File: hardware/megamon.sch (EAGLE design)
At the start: 76 parts

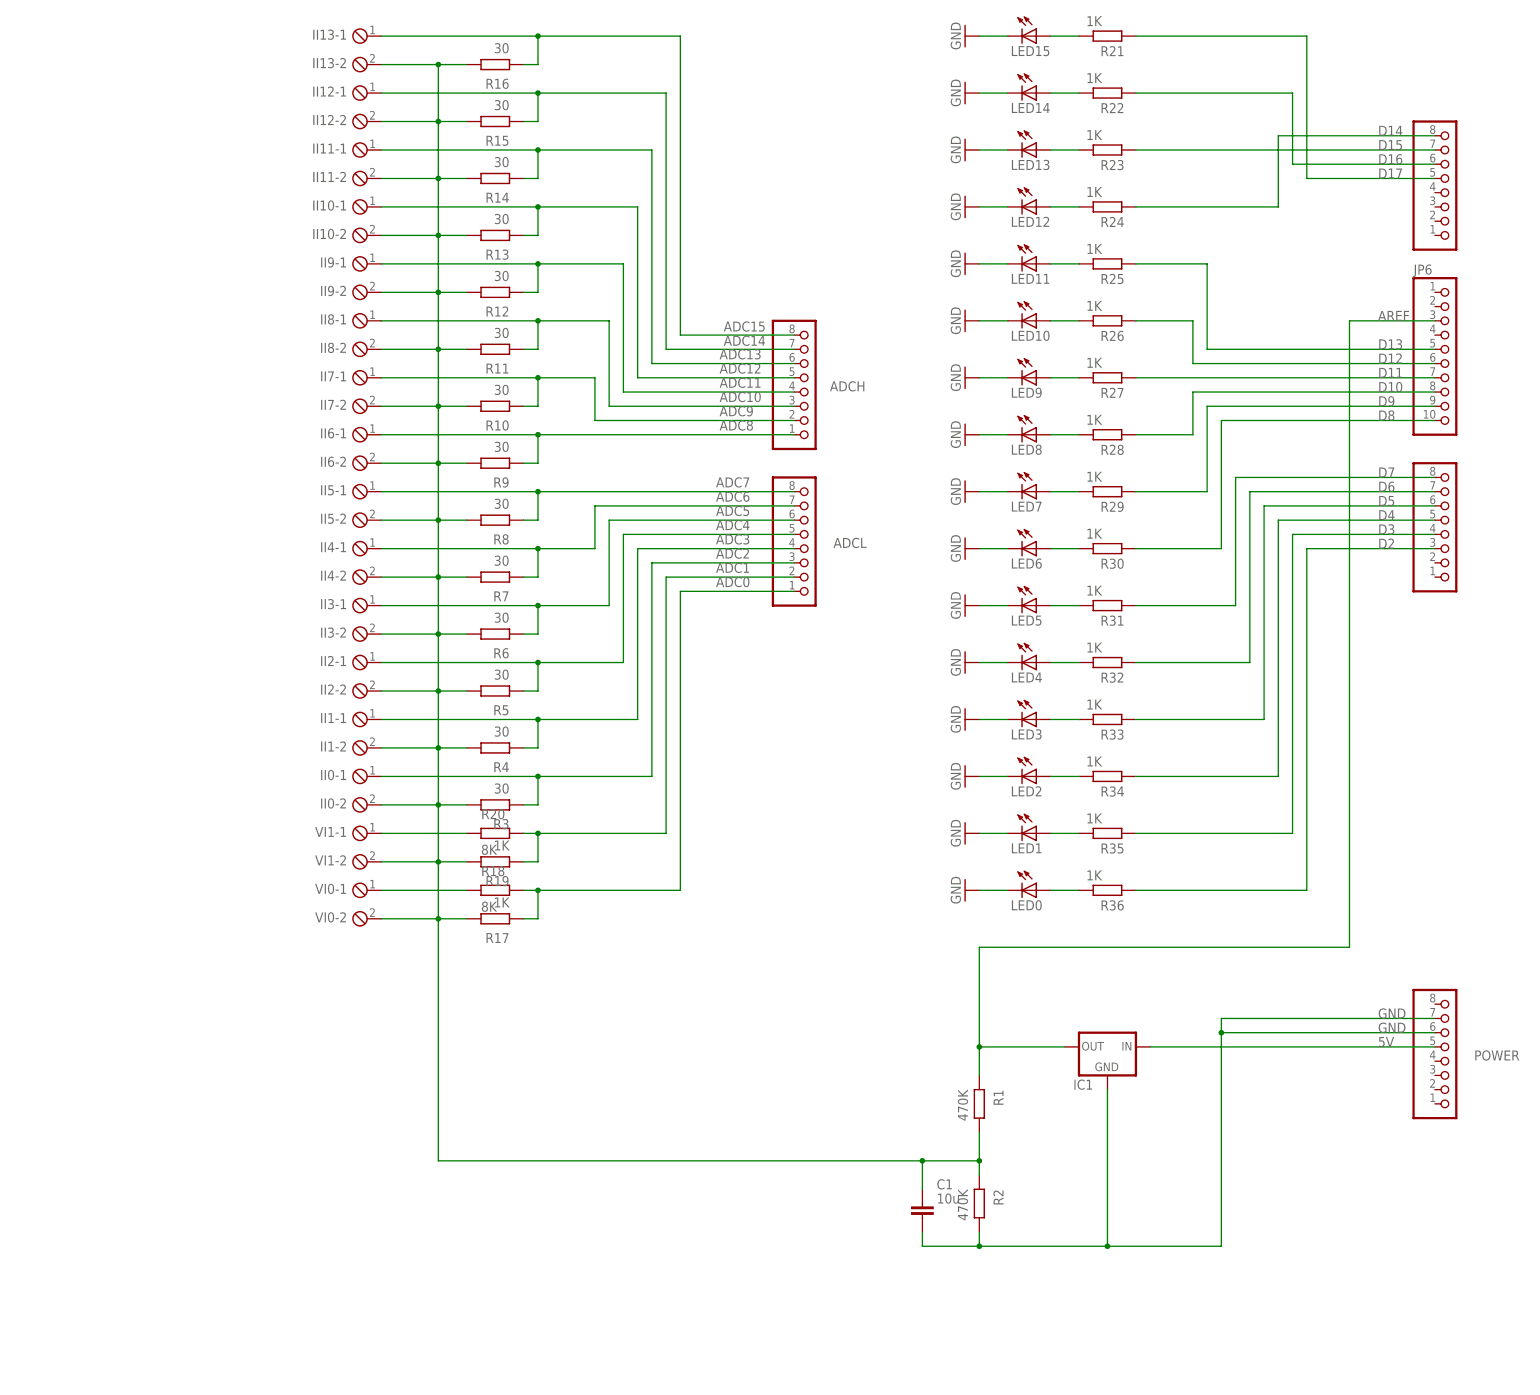
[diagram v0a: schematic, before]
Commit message: replace ngspice components with real ones
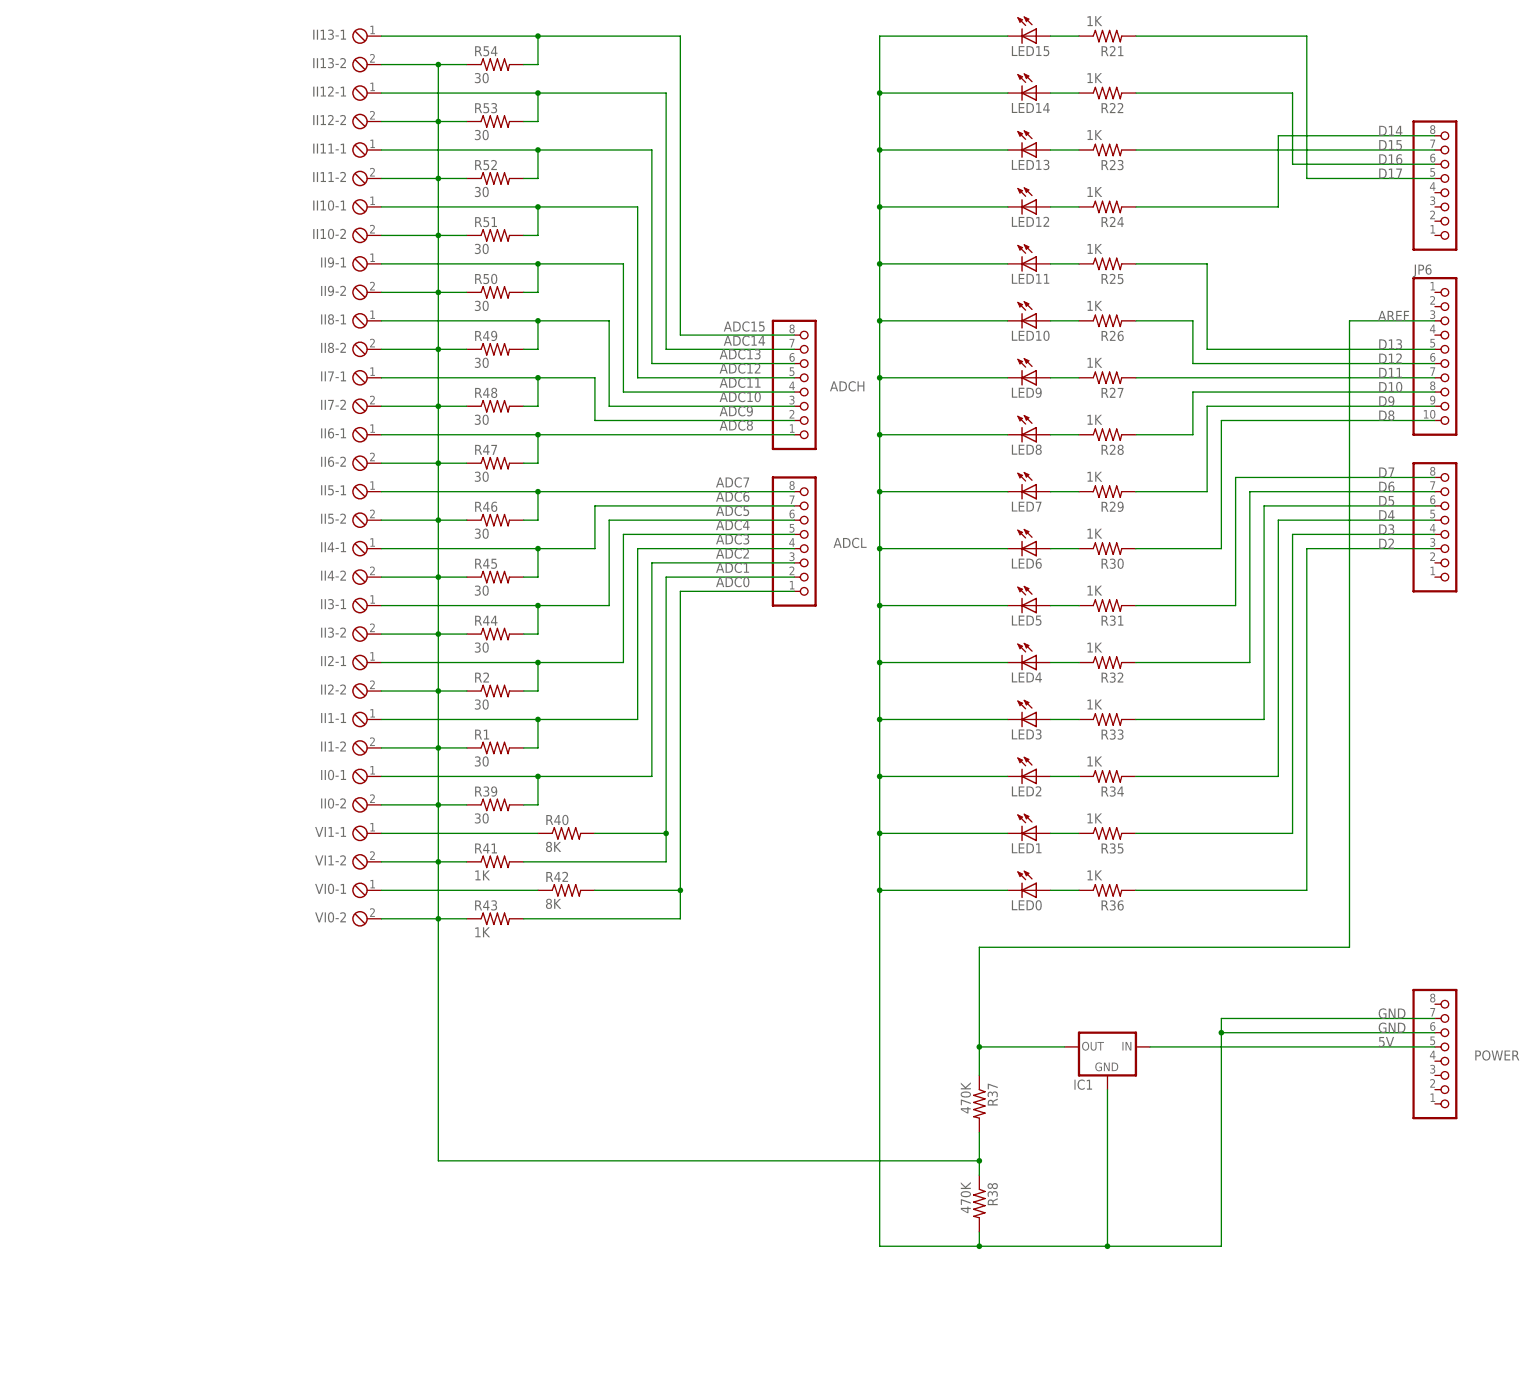
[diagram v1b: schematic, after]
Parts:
- removed C1: 10u, ngspice-simulation:C
- removed R10, R11, R12, R13, R14, R15, R16, R3, R4, R5, R6, R7, R8, R9: 30, ngspice-simulation:R
- removed R17, R19: 1K, ngspice-simulation:R
- removed R18, R20: 8K, ngspice-simulation:R
- added R37, R38: 470K, rcl:R-US_0204/7
- added R39, R44, R45, R46, R47, R48, R49, R50, R51, R52, R53, R54: 30, rcl:R-US_0204/7
- added R40, R42: 8K, rcl:R-US_0204/7
- added R41, R43: 1K, rcl:R-US_0204/7
- LED0, LED1, LED10, LED11, LED12, LED13, LED14, LED15, LED2, LED3, LED4, LED5, LED6, LED7, LED8, LED9: device led:LEDCHIPLED_0805 -> adafruit:LED3MM
- R1, R2: value 470K -> 30; device ngspice-simulation:R -> rcl:R-US_0204/7
- R21, R22, R23, R24, R25, R26, R27, R28, R29, R30, R31, R32, R33, R34, R35, R36: device rcl:R-EU_R0603 -> rcl:R-US_0204/7
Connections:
- net ADC0: now also R42.2, R43.2; no longer R17.1, R18.2
- net ADC1: now also R40.2, R41.2; no longer R19.1, R20.2
- net ADC10: now also R49.2; no longer R11.1
- net ADC11: now also R50.2; no longer R12.1
- net ADC12: now also R51.2; no longer R13.1
- net ADC13: now also R52.2; no longer R14.1
- net ADC14: now also R53.2; no longer R15.1
- net ADC15: now also R54.2; no longer R16.1
- net ADC2: now also R39.2; no longer R3.1
- net ADC3: now also R1.2; no longer R4.1
- net ADC4: now also R2.2; no longer R5.1
- net ADC5: now also R44.2; no longer R6.1
- net ADC6: now also R45.2; no longer R7.1
- net ADC7: now also R46.2; no longer R8.1
- net ADC8: now also R47.2; no longer R9.1
- net ADC9: now also R48.2; no longer R10.1
- net AREF: now also R37.1; no longer R1.1
- net GND: now also R38.2; no longer C1.2, R2.2
- net N$2: now also R40.1; no longer R20.1
- net N$6: now also R42.1; no longer R18.1
- net V_MID: now also R1.1, R37.2, R38.1, R39.1, R41.1, R43.1, R44.1, R45.1, R46.1, R47.1, R48.1, R49.1, R50.1, R51.1, R52.1, R53.1, R54.1; no longer C1.1, R1.2, R10.2, R11.2, R12.2, R13.2, R14.2, R15.2, R16.2, R17.2, R19.2, R3.2, R4.2, R5.2, R6.2, R7.2, R8.2, R9.2

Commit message: removed all but one LED
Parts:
- removed LED0, LED1, LED10, LED11, LED12, LED13, LED14, LED15, LED2, LED3, LED4, LED5, LED6, LED8, LED9: green, adafruit:LED3MM
- removed R21, R22, R23, R24, R25, R26, R27, R28, R30, R31, R32, R33, R34, R35, R36: 1K, rcl:R-US_0204/7
- added NEG_1, NEG_2, POS_1, POS_2: (no value), con-phoenix-254:MPT8
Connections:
- removed net D10: JP6.8, R28.2
- removed net D11: JP6.7, R27.2
- removed net D12: JP6.6, R26.2
- removed net D13: JP6.5, R25.2
- removed net D14: COMMUNICATION.8, R24.2
- removed net D15: COMMUNICATION.7, R23.2
- removed net D16: COMMUNICATION.6, R22.2
- removed net D17: COMMUNICATION.5, R21.2
- removed net D2: PWML.3, R36.2
- removed net D3: PWML.4, R35.2
- removed net D4: PWML.5, R34.2
- removed net D5: PWML.6, R33.2
- removed net D6: PWML.7, R32.2
- removed net D7: PWML.8, R31.2
- removed net D8: JP6.10, R30.2
- removed net N$10: LED8.A, R28.1
- removed net N$12: LED6.A, R30.1
- removed net N$13: LED5.A, R31.1
- removed net N$14: LED4.A, R32.1
- removed net N$15: LED3.A, R33.1
- removed net N$16: LED2.A, R34.1
- removed net N$17: LED1.A, R35.1
- removed net N$18: LED0.A, R36.1
- removed net N$3: LED14.A, R22.1
- removed net N$4: LED13.A, R23.1
- removed net N$41: LED15.A, R21.1
- removed net N$5: LED12.A, R24.1
- removed net N$7: LED11.A, R25.1
- removed net N$8: LED10.A, R26.1
- removed net N$9: LED9.A, R27.1
- net GND: no longer LED0.C, LED1.C, LED10.C, LED11.C, LED12.C, LED13.C, LED14.C, LED15.C, LED2.C, LED3.C, LED4.C, LED5.C, LED6.C, LED8.C, LED9.C
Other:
- moved on the sheet: JP6, LED7, R29

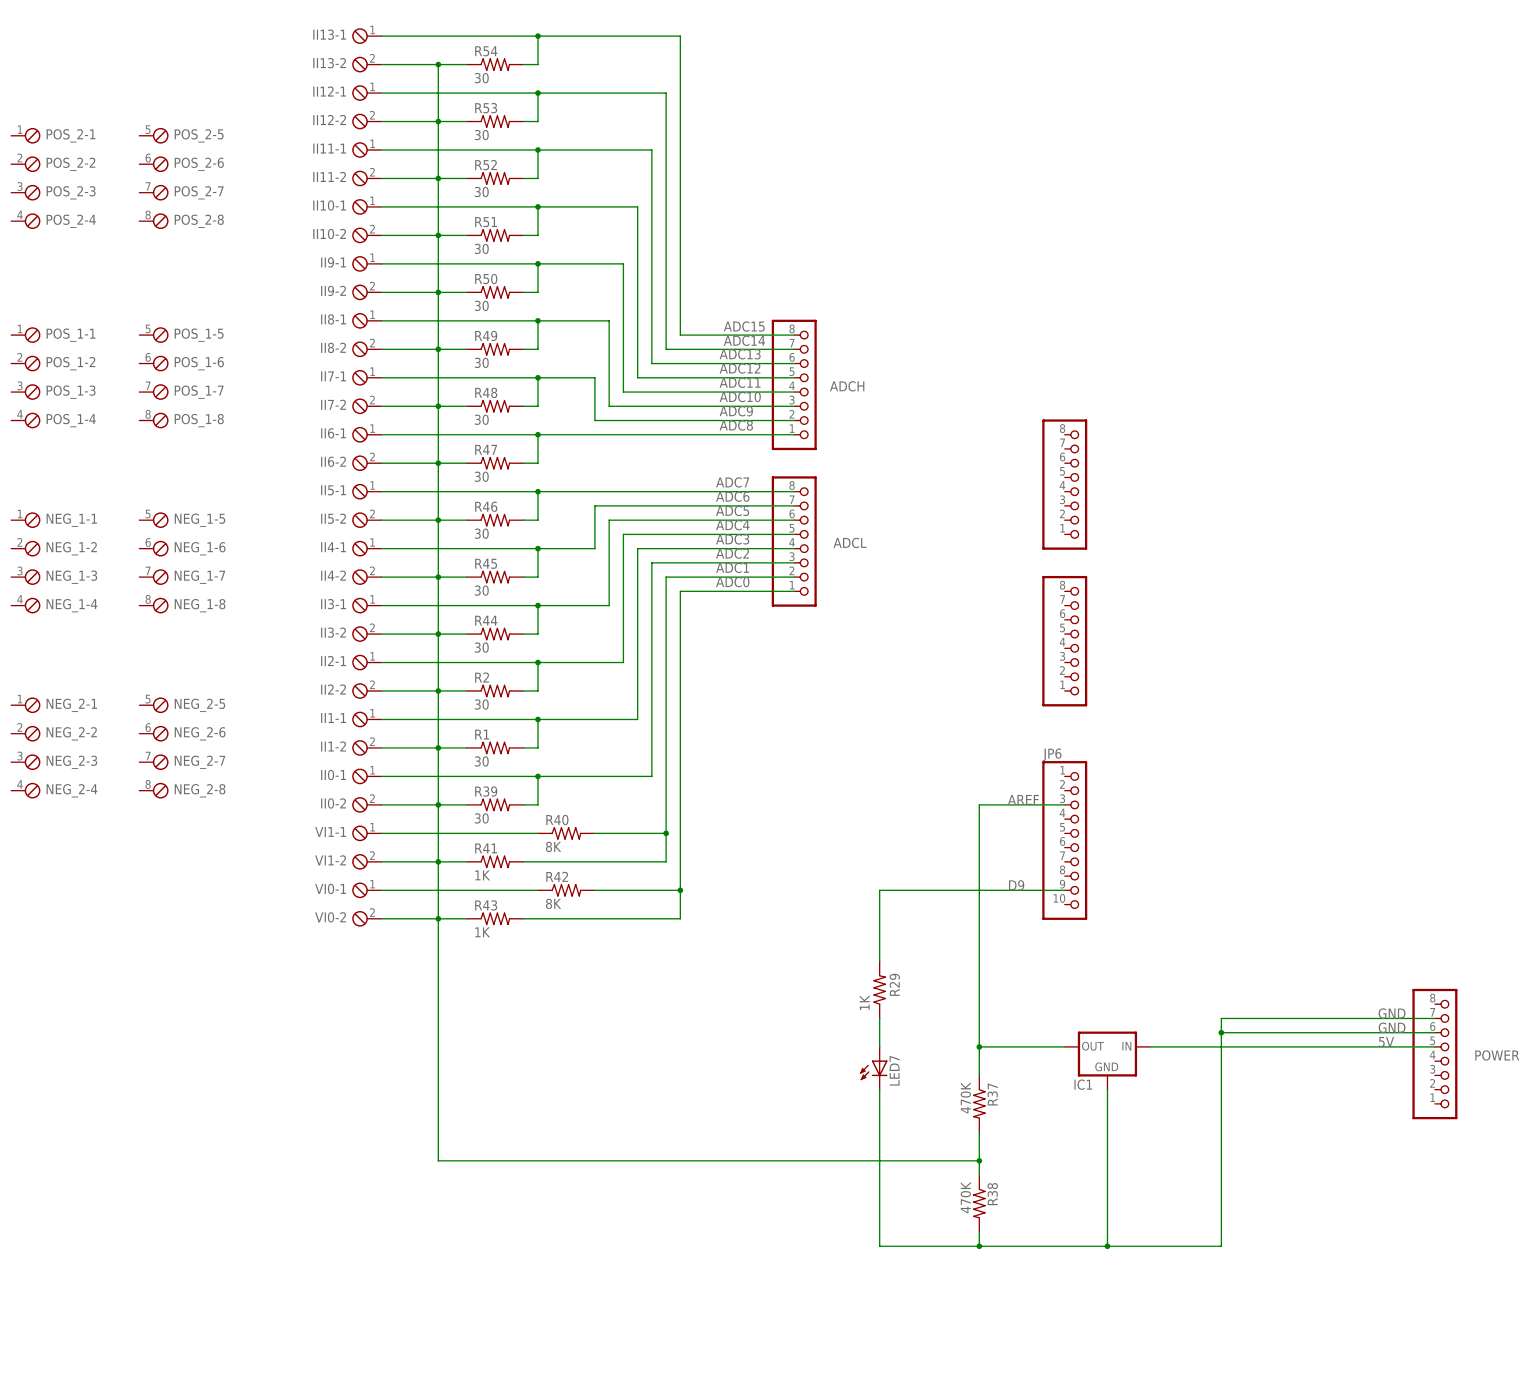
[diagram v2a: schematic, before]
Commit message: replace pair terminals with separate pos/neg
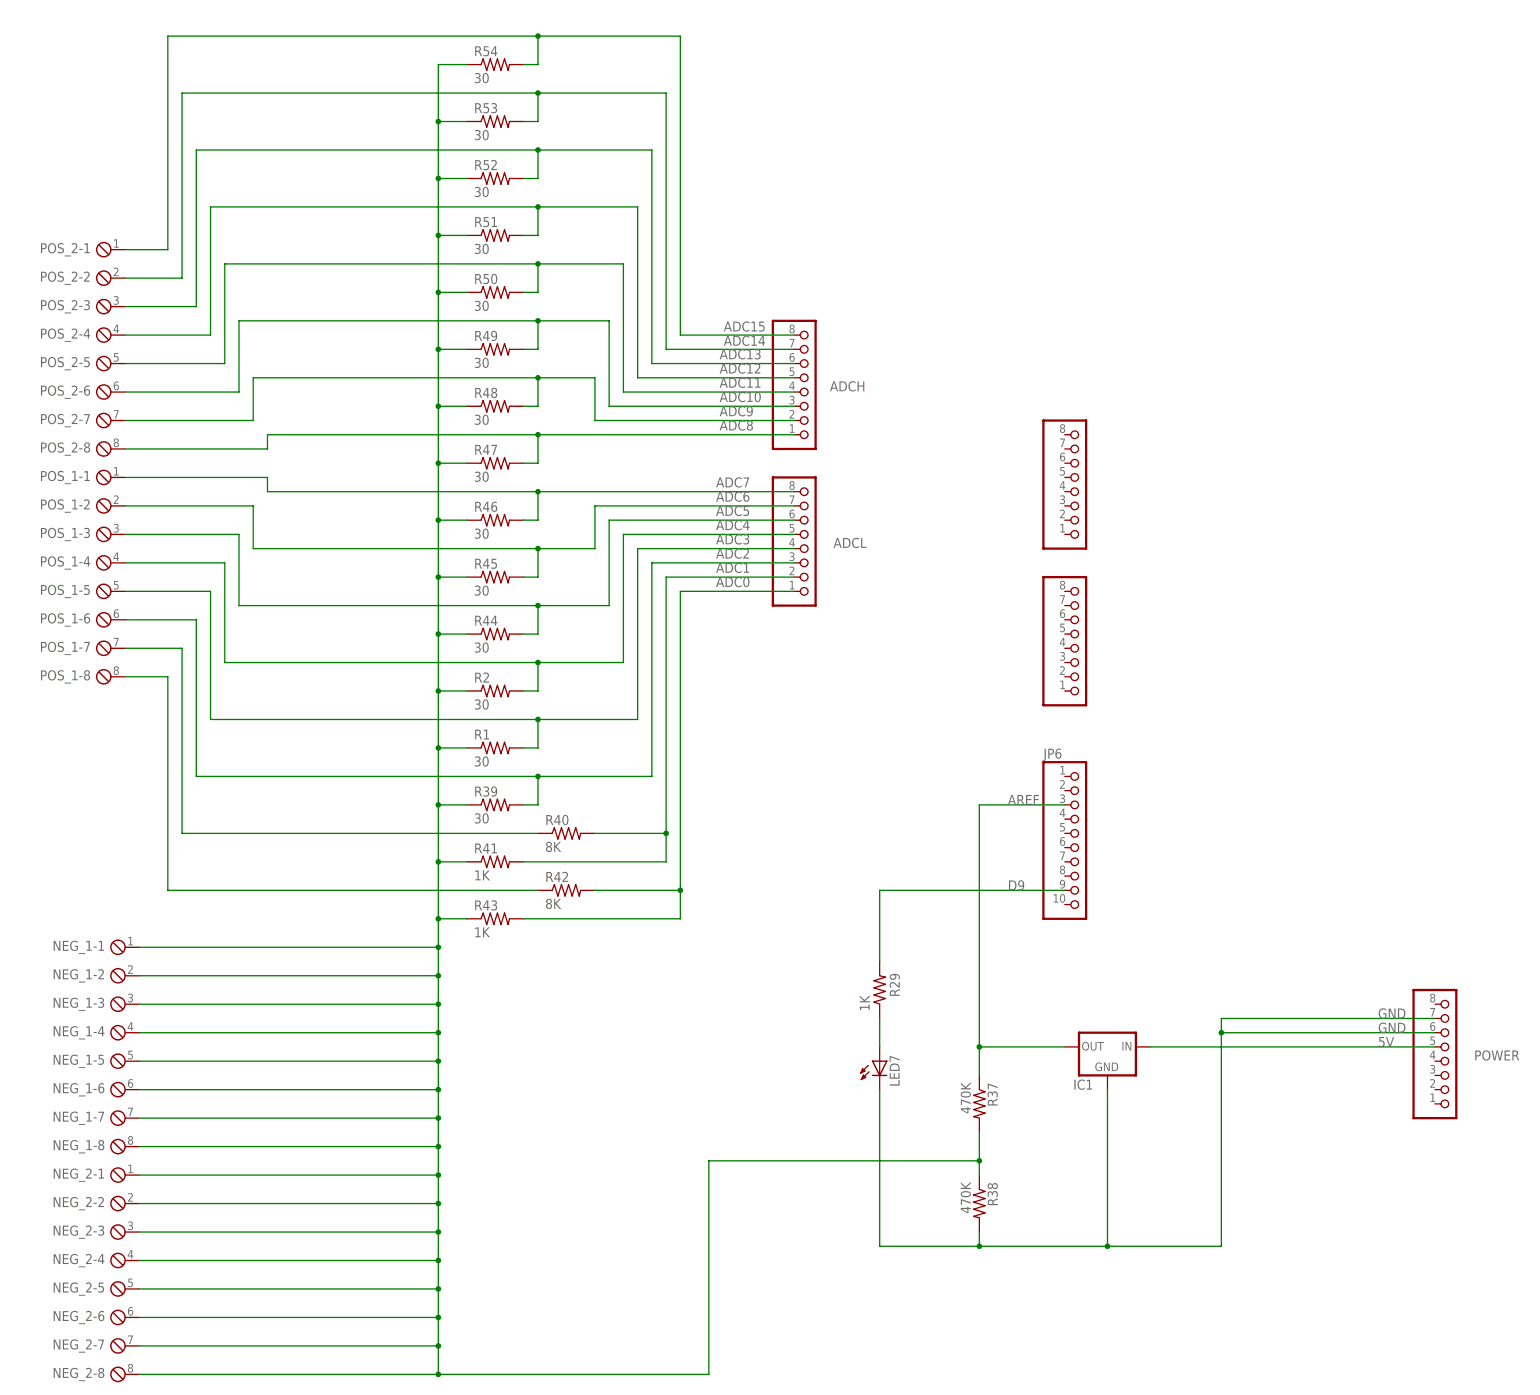
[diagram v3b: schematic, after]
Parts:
- removed II0, II1, II10, II11, II12, II13, II2, II3, II4, II5, II6, II7, II8, II9, VI0, VI1: (no value), con-phoenix-254:MPT2
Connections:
- net ADC10: now also POS_2-6.1; no longer II8-1.1
- net ADC11: now also POS_2-5.1; no longer II9-1.1
- net ADC12: now also POS_2-4.1; no longer II10-1.1
- net ADC13: now also POS_2-3.1; no longer II11-1.1
- net ADC14: now also POS_2-2.1; no longer II12-1.1
- net ADC15: now also POS_2-1.1; no longer II13-1.1
- net ADC2: now also POS_1-6.1; no longer II0-1.1
- net ADC3: now also POS_1-5.1; no longer II1-1.1
- net ADC4: now also POS_1-4.1; no longer II2-1.1
- net ADC5: now also POS_1-3.1; no longer II3-1.1
- net ADC6: now also POS_1-2.1; no longer II4-1.1
- net ADC7: now also POS_1-1.1; no longer II5-1.1
- net ADC8: now also POS_2-8.1; no longer II6-1.1
- net ADC9: now also POS_2-7.1; no longer II7-1.1
- net N$2: now also POS_1-7.1; no longer VI1-1.1
- net N$6: now also POS_1-8.1; no longer VI0-1.1
- net V_MID: now also NEG_1-1.1, NEG_1-2.1, NEG_1-3.1, NEG_1-4.1, NEG_1-5.1, NEG_1-6.1, NEG_1-7.1, NEG_1-8.1, NEG_2-1.1, NEG_2-2.1, NEG_2-3.1, NEG_2-4.1, NEG_2-5.1, NEG_2-6.1, NEG_2-7.1, NEG_2-8.1; no longer II0-2.1, II1-2.1, II10-2.1, II11-2.1, II12-2.1, II13-2.1, II2-2.1, II3-2.1, II4-2.1, II5-2.1, II6-2.1, II7-2.1, II8-2.1, II9-2.1, VI0-2.1, VI1-2.1
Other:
- moved on the sheet: NEG_1-1, NEG_1-2, NEG_1-3, NEG_1-4, NEG_1-5, NEG_1-6, NEG_1-7, NEG_1-8, NEG_2-1, NEG_2-2, NEG_2-3, NEG_2-4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
